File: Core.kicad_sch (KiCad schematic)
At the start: 14 parts, among them J4 Conn_ARM_JTAG_SWD_10, U4 X1000, X1 SG-3030CM, Y2 24MHz

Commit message: Update (Display)
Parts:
- R26, R27, R28, R29, R30, R31: footprint (none) -> Resistor_SMD:R_0402_1005Metric
- U4: footprint (none) -> TheBrutzlers_Lib:BGA256C80P16X16_1300X1300X130N
- renumbered C62 to C63, C63 to C64, C64 to C65
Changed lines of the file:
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@@
     (property "Reference" "U4" (id 0) (at 137.16 44.45 0))
     (property "Value" "X1000" (id 1) (at 137.16 46.99 0))
-    (property "Footprint" "" (id 2) (at 125.73 62.23 0)
+    (property "Footprint" "TheBrutzlers_Lib:BGA256C80P16X16_1300X1300X130N" (id 2) (at 125.73 62.23 0)
       (effects (font (size 1.27 1.27)) (justify left) hide)
     )
@@
   (symbol (lib_id "Device:C") (at 96.52 64.77 90) (unit 1)
     (in_bom yes) (on_board yes)
-    (property "Reference" "C64" (id 0) (at 93.98 63.5 90))
+    (property "Reference" "C65" (id 0) (at 93.98 63.5 90))
     (property "Value" "C" (id 1) (at 99.06 63.5 90))
     (property "Footprint" "Capacitor_SMD:C_0402_1005Metric" (id 2) (at 100.33 63.8048 0)
@@
       (effects (font (size 1.27 1.27)) (justify left))
     )
-    (property "Footprint" "" (id 2) (at 193.802 85.09 90)
+    (property "Footprint" "Resistor_SMD:R_0402_1005Metric" (id 2) (at 193.802 85.09 90)
       (effects (font (size 1.27 1.27)) hide)
     )
@@
       (effects (font (size 1.27 1.27)) (justify left))
     )
-    (property "Footprint" "" (id 2) (at 183.642 85.09 90)
+    (property "Footprint" "Resistor_SMD:R_0402_1005Metric" (id 2) (at 183.642 85.09 90)
       (effects (font (size 1.27 1.27)) hide)
     )
@@
       (effects (font (size 1.27 1.27)) (justify left))
     )
-    (property "Footprint" "" (id 2) (at 183.642 71.12 90)
+    (property "Footprint" "Resistor_SMD:R_0402_1005Metric" (id 2) (at 183.642 71.12 90)
       (effects (font (size 1.27 1.27)) hide)
     )
@@
   (symbol (lib_id "Device:C") (at 59.69 59.69 90) (unit 1)
     (in_bom yes) (on_board yes)
-    (property "Reference" "C62" (id 0) (at 55.88 58.42 90))
+    (property "Reference" "C63" (id 0) (at 55.88 58.42 90))
     (property "Value" "C" (id 1) (at 62.23 58.42 90))
     (property "Footprint" "Capacitor_SMD:C_0402_1005Metric" (id 2) (at 63.5 58.7248 0)
@@
   (symbol (lib_id "Device:C") (at 59.69 69.85 90) (unit 1)
     (in_bom yes) (on_board yes)
-    (property "Reference" "C63" (id 0) (at 55.88 71.12 90))
+    (property "Reference" "C64" (id 0) (at 55.88 71.12 90))
     (property "Value" "C" (id 1) (at 62.23 71.12 90))
     (property "Footprint" "Capacitor_SMD:C_0402_1005Metric" (id 2) (at 63.5 68.8848 0)
@@
       (effects (font (size 1.27 1.27)) (justify left))
     )
-    (property "Footprint" "" (id 2) (at 188.722 85.09 90)
+    (property "Footprint" "Resistor_SMD:R_0402_1005Metric" (id 2) (at 188.722 85.09 90)
       (effects (font (size 1.27 1.27)) hide)
     )
@@
       (effects (font (size 1.27 1.27)) (justify left))
     )
-    (property "Footprint" "" (id 2) (at 193.802 71.12 90)
+    (property "Footprint" "Resistor_SMD:R_0402_1005Metric" (id 2) (at 193.802 71.12 90)
       (effects (font (size 1.27 1.27)) hide)
     )
@@
       (effects (font (size 1.27 1.27)) (justify left))
     )
-    (property "Footprint" "" (id 2) (at 188.722 71.12 90)
-      (effects (font (size 1.27 1.27)) hide)
-    )
+    (property "Footprint" "Resistor_SMD:R_0402_1005Metric" (id 2) (at 188.722 71.12 90)
+      (effects (font (size 1.27 1.27)) hide)
+    )

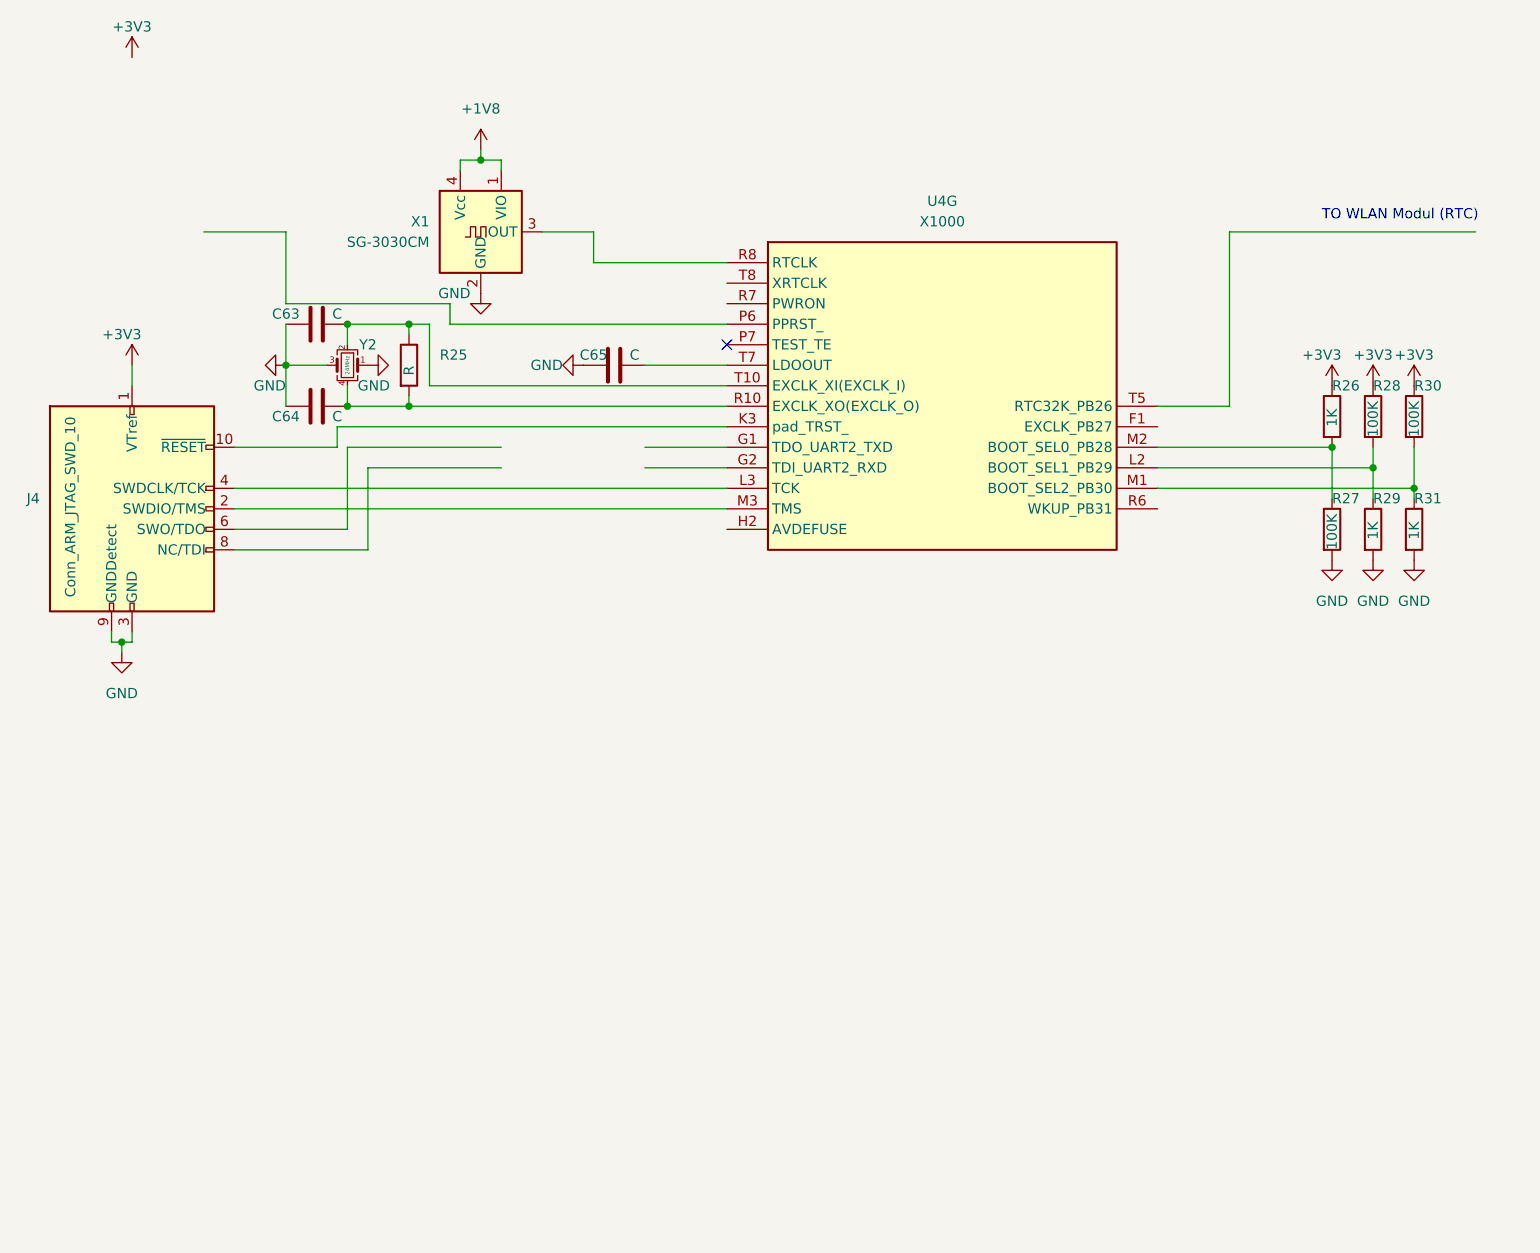
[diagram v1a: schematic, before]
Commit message: Add Audio
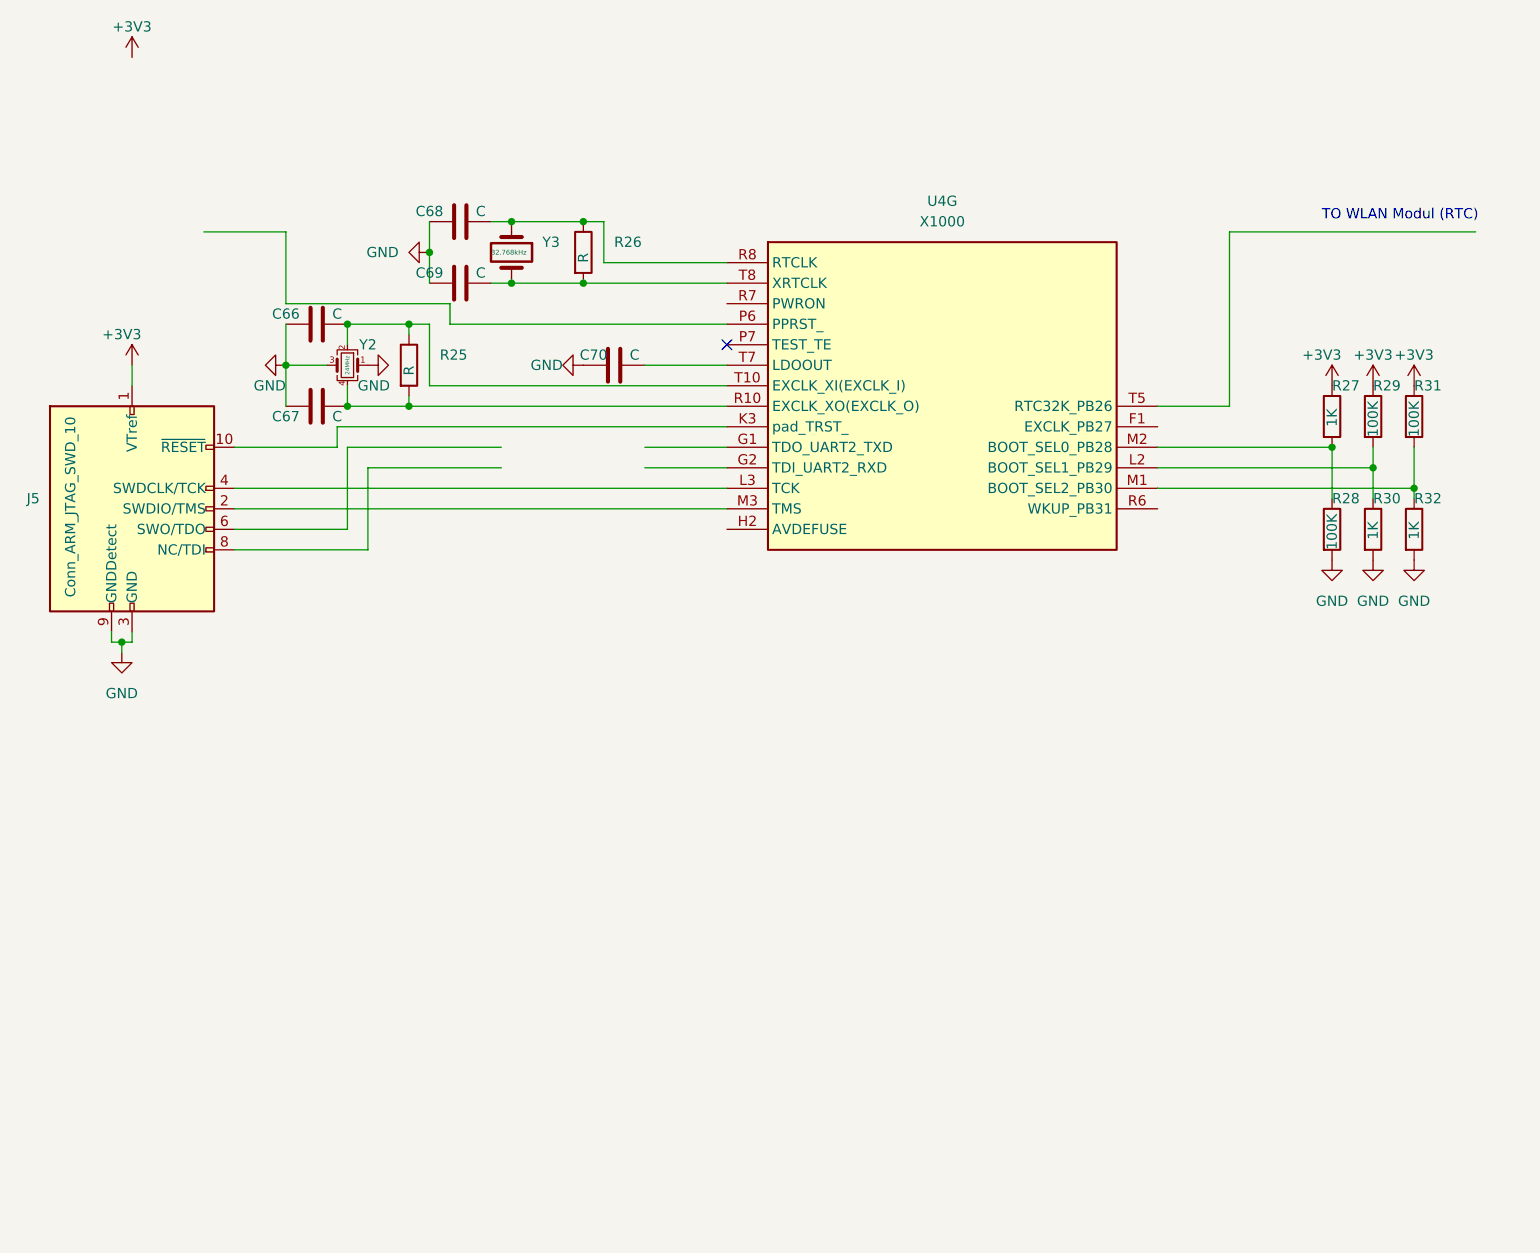
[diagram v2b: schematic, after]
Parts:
- removed X1: SG-3030CM, Oscillator:Oscillator_SMD_SeikoEpson_SG3030CM, symbol Oscillator:SG-3030CM
- added C68, C69: C, Capacitor_SMD:C_0402_1005Metric, symbol Device:C
- added R26: R, symbol Device:R
- added Y3: 32.768kHz, Crystal:Crystal_C26-LF_D2.1mm_L6.5mm_Horizontal, symbol Device:Crystal
- Y2: footprint (none) -> Crystal:Crystal_SMD_ECS_CSM3X-2Pin_7.6x4.1mm; LCSC (none) -> C555584
- renumbered C63 to C66, C64 to C67, C65 to C70, J4 to J5, R26 to R27, R27 to R28, R28 to R29, R29 to R30, R30 to R31, R31 to R32
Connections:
- net GND: now also C68.1, C69.1
- net at U4.R8 (RTCLK): now also C68.2, R26.1, Y3.1
- net at U4.T8 (XRTCLK): now also C69.2, R26.2, Y3.2

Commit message: New i.mx6 Version
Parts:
- added U? (x2): IMX6UL, TheBrutzlers_Lib:IMX6UL_BGA289, symbol TheBrutzlers_Lib:IMX6UL

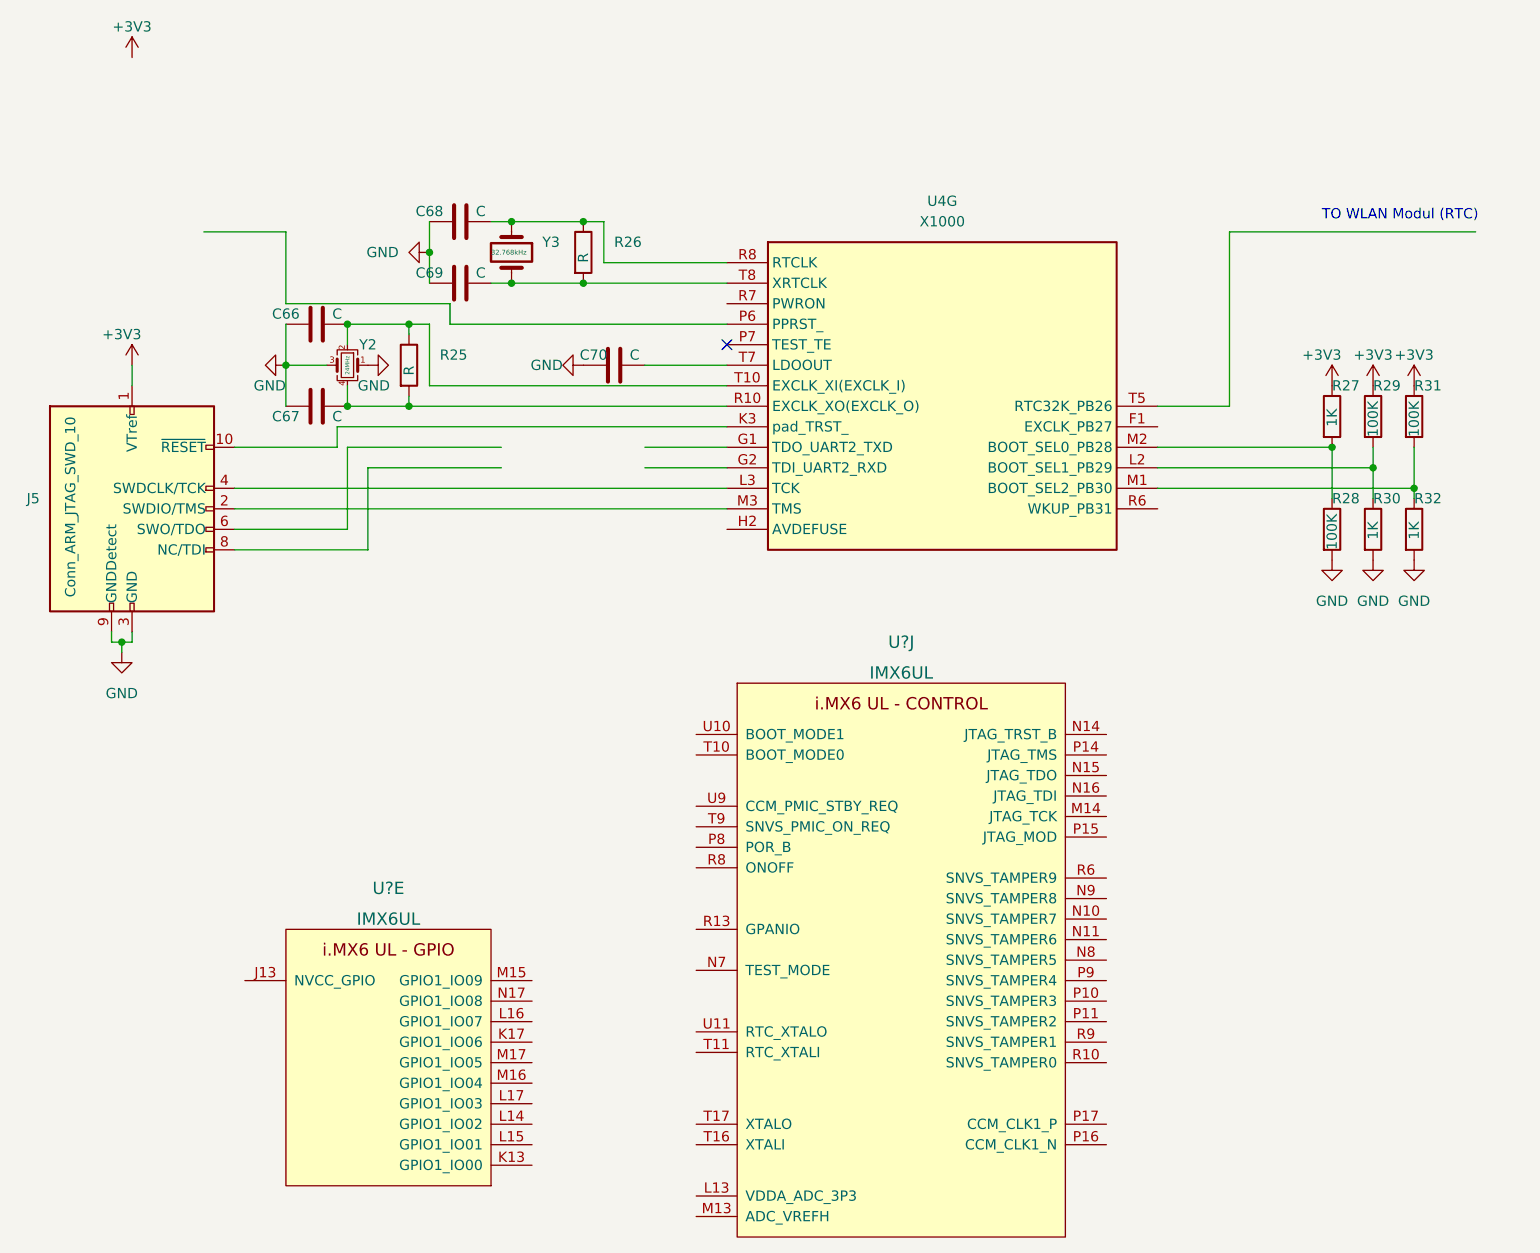
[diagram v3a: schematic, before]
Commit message: Display Update
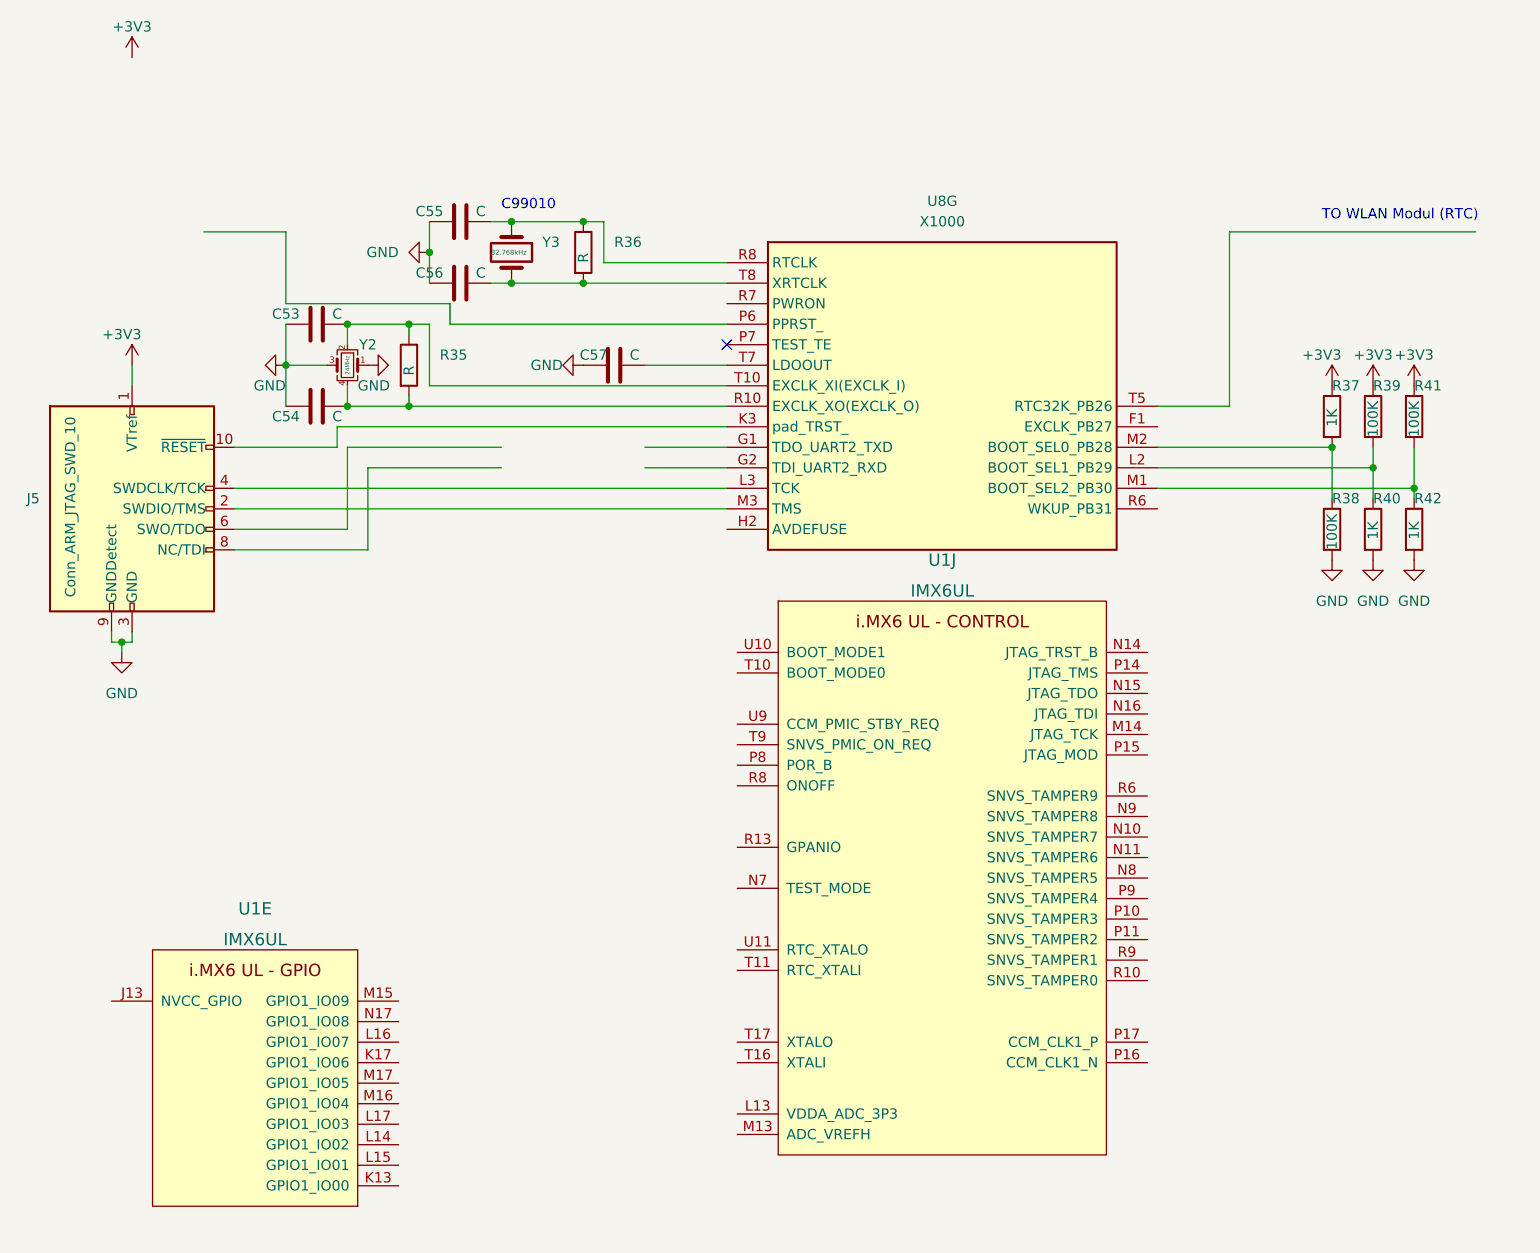
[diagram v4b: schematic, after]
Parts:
- gave numbers to parts that had none: 1
- renumbered C66 to C53, C67 to C54, C68 to C55, C69 to C56, C70 to C57, R25 to R35, R26 to R36, R27 to R37, R28 to R38, R29 to R39, R30 to R40, R31 to R41, R32 to R42, U4 to U8
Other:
- note added: "C99010"
- moved on the sheet: U1E, U1J
